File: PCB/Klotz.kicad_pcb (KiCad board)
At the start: 2 copper layers, 120.5 x 85.5 mm, 56 parts, among them SW1 MX_SW_HS, SW10 MX_SW_HS, SW11 MX_SW_HS, SW12 MX_SW_HS, SW13 MX_SW_HS, SW14 MX_SW_HS, SW15 MX_SW_HS, SW16 MX_SW_HS, SW17 MX_SW_HS, SW18 RotaryEncoder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

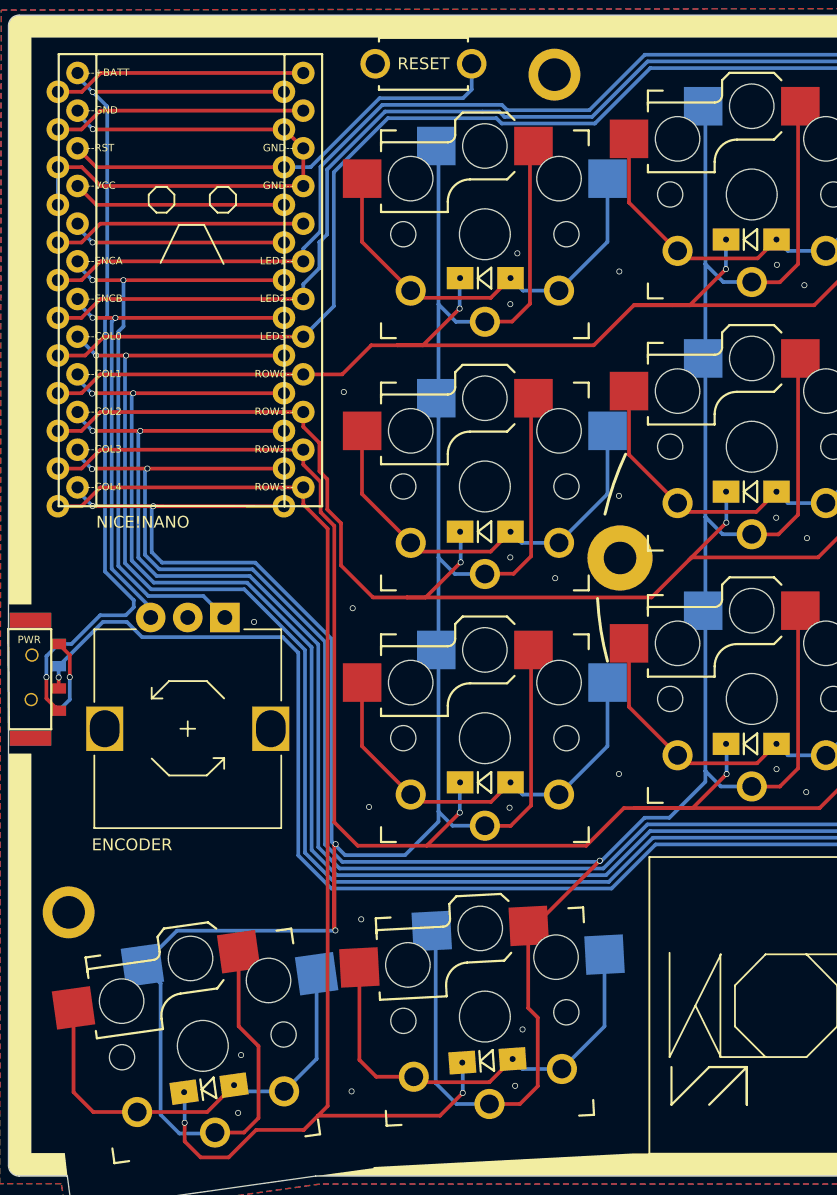
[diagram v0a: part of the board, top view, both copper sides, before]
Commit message: Tweak PCB with more cosmetic changes.
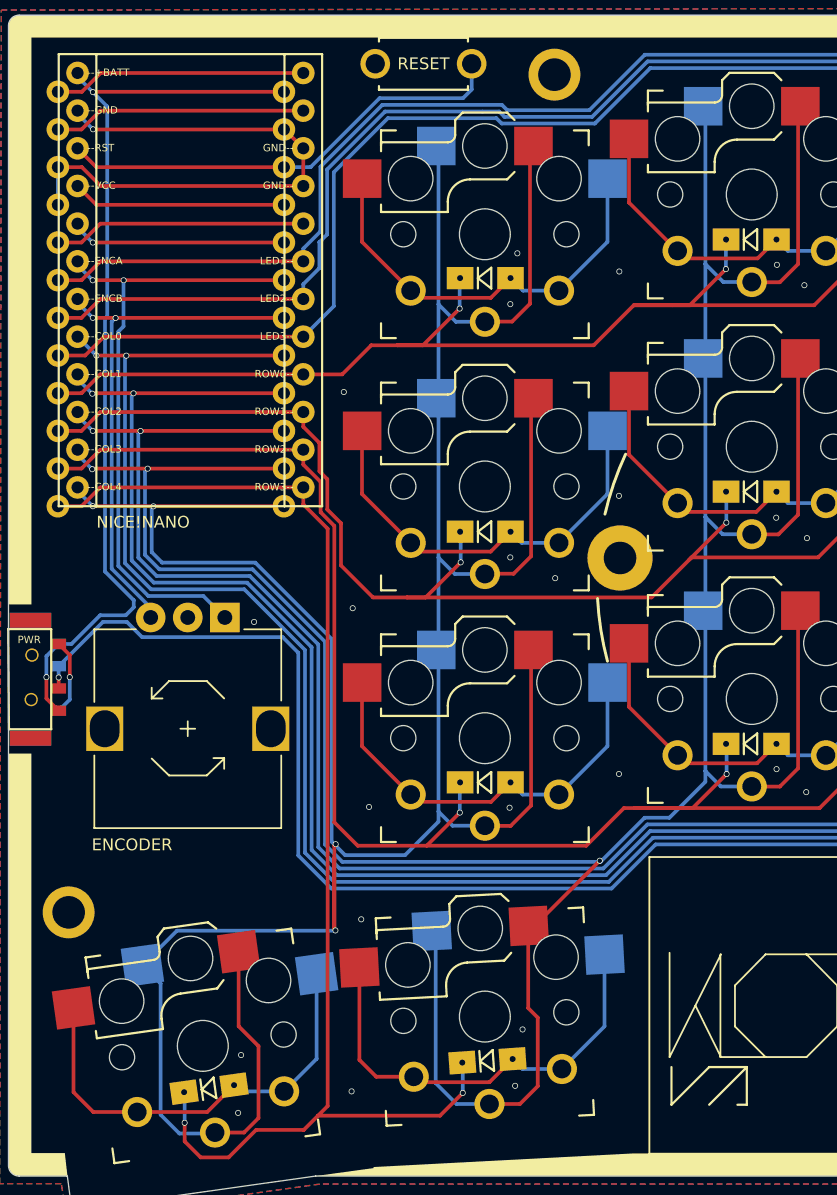
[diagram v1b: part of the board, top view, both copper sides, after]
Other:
- board text added: "--3.3V"
- board text added: "--COLO"
